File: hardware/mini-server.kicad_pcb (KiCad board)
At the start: 6 copper layers, 91 parts, among them J1 RJ45_Hanrun_HR911105A_Horizon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, J2 HDMI_A, J3 Micro_SD_Card, J5 AudioJack4, J6 USB_C_Receptacle, J7 USB_C_Receptacle, J8 USB_C_Receptacle, Q1 2N7002, U1 NT5CB256M16ER-FL, U2 RK3328, U3 TPD12S016PWR, U6 TPS563252DRLR, U7 TPS563252DRLR, U8 TPS563252DRLR, U9 TPS563252DRLR

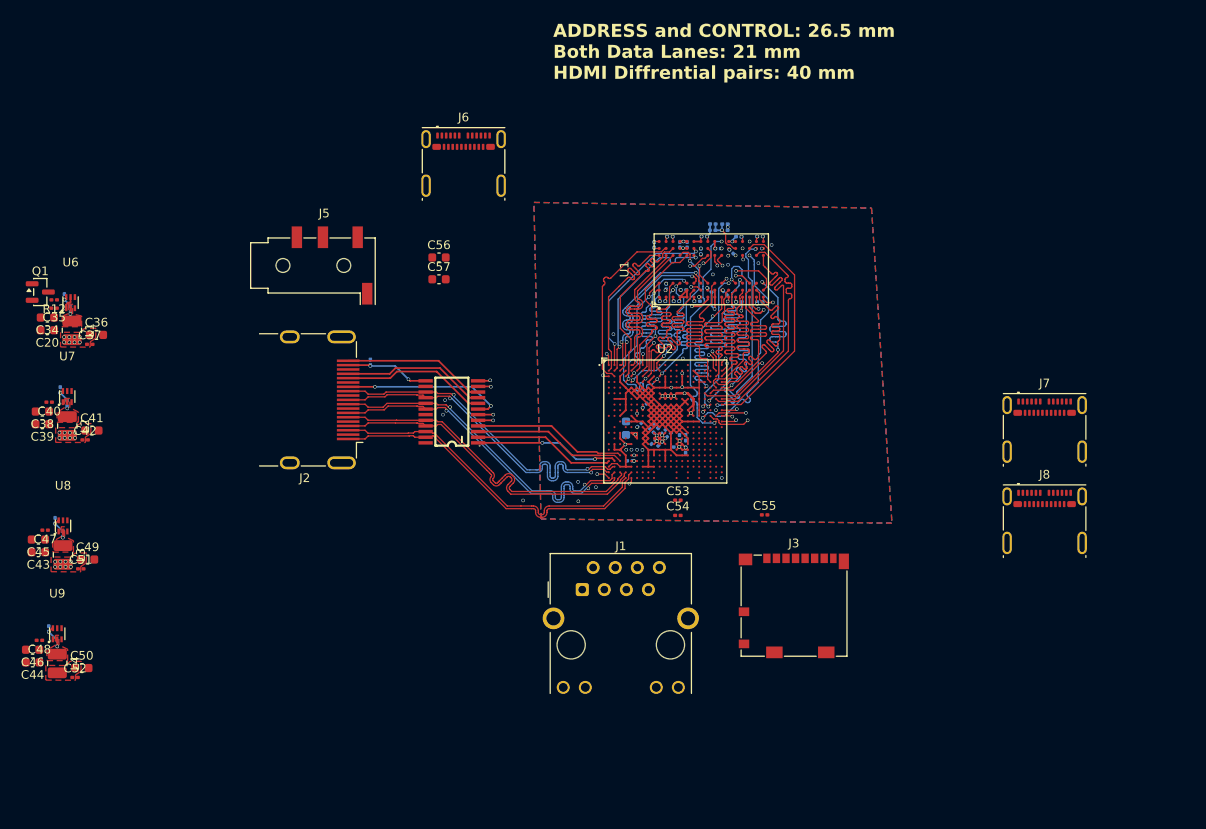
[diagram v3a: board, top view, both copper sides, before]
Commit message: component Placement
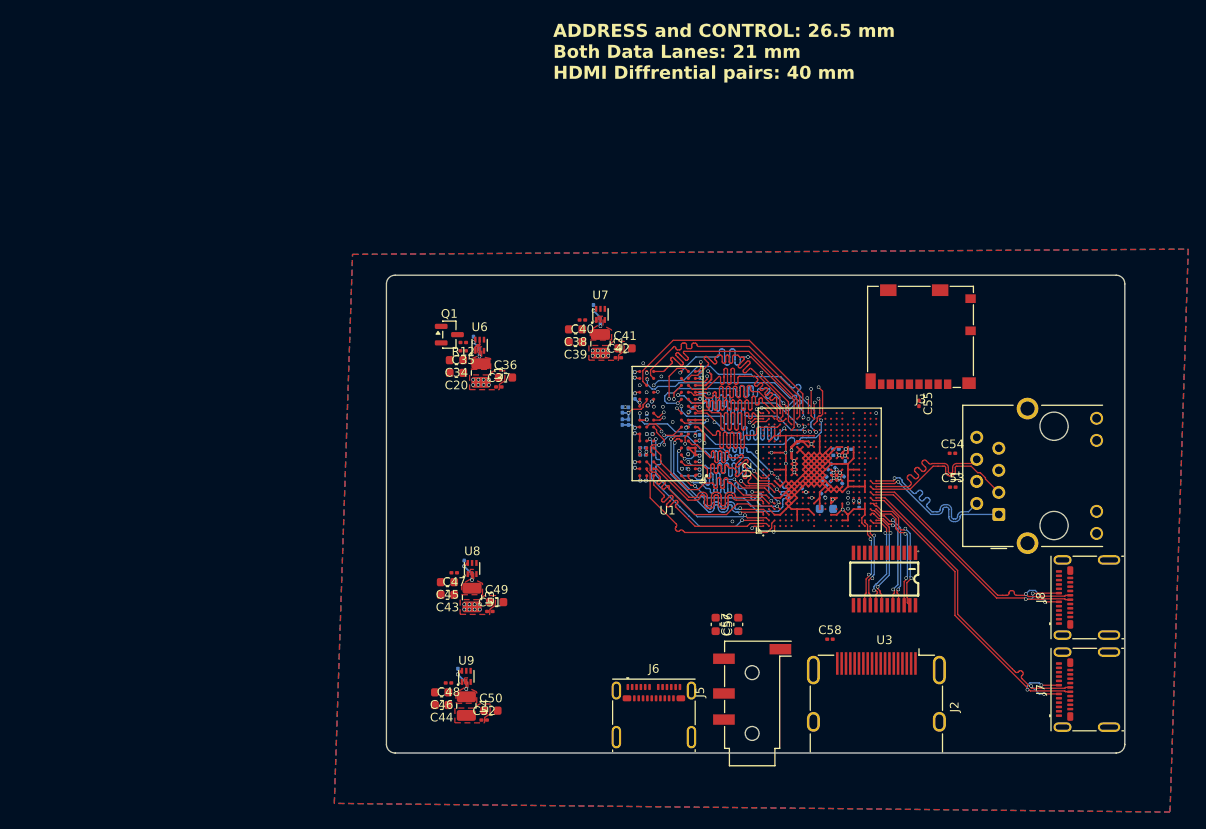
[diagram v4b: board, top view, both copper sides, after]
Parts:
- C58: moved to F.Cu
- moved J2 72.4 mm to (153.9, 122.4), turned to -90 degrees
- moved J5 69.6 mm to (139.6, 122.4), turned to 90 degrees
- moved J6 67.2 mm to (128.3, 125.0)
- moved C38 62.1 mm to (119.3, 80.6)
- moved C39 62.1 mm to (119.3, 82.1)
- moved C40 62.1 mm to (120.1, 79.6)
- moved U7 62.1 mm to (122.1, 78.9)
- moved C41 62.1 mm to (125.0, 82.8)
- moved C42 62.1 mm to (124.2, 83.9)
- moved L2 62.1 mm to (122.1, 82.3)
- moved R6 62.1 mm to (122.1, 79.7)
- moved R7 62.1 mm to (121.3, 78.2)
- moved C58 61.8 mm to (148.6, 116.3), turned to 0 degrees
- moved U3 53.4 mm to (154.8, 109.4), turned to 180 degrees
- moved C56 52.9 mm to (135.4, 114.6), turned to -90 degrees
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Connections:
- net /USB/USB2_0_DM renamed /USB/USB2_0_D-
- net /USB/USB2_0_DP renamed /USB/USB2_0_D+
- net /USB/USB2_1_DM renamed /USB/USB2_1_D-
- net /USB/USB2_1_DP renamed /USB/USB2_1_D+
- J7 pad A4: Net-(J7-VBUS-PadA4) -> VSYS
- J7 pad A9: Net-(J7-VBUS-PadA4) -> VSYS
- J7 pad B4: Net-(J7-VBUS-PadA4) -> VSYS
- J7 pad B9: Net-(J7-VBUS-PadA4) -> VSYS
- J8 pad A1: Net-(J8-GND-PadA1) -> GND
- J8 pad A12: Net-(J8-GND-PadA1) -> GND
- J8 pad B1: Net-(J8-GND-PadA1) -> GND
- J8 pad B12: Net-(J8-GND-PadA1) -> GND
- J8 pad SH: unconnected-(J8-SHIELD-PadSH) -> GND
- U1 pad J1: GND -> unconnected-(U1-NC-PadJ1)
- U2 pad AA15: unconnected-(U2E-GPIO1_B1/UART0_TX/GMAC_TXD0_M1-PadAA15) -> Net-(J4-Pin_2)
- U2 pad R1: unconnected-(U2H-XIN24M-PadR1) -> Net-(U2H-XIN24M)
- U2 pad T1: unconnected-(U2H-XOUT24M-PadT1) -> Net-(U2H-XOUT24M)
- U2 pad V13: unconnected-(U2E-GPIO1_B3/UART0_CTSN/GMAC_RXD0_M1-PadV13) -> Net-(U2E-GPIO1_B3/UART0_CTSN/GMAC_RXD0_M1)
- U2 pad W14: unconnected-(U2E-GPIO1_B2/UART0_RTSN/GMAC_RXD1_M1-PadW14) -> Net-(U2E-GPIO1_B2/UART0_RTSN/GMAC_RXD1_M1)
- U2 pad Y15: unconnected-(U2E-GPIO1_B0/UART0_RX/GMAC_TXD1_M1-PadY15) -> Net-(J4-Pin_3)
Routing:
- net /USB/USB2_0_D-: track 0.00 -> 39.7 mm, vias 0 -> 2
- net /USB/USB2_0_D+: track 0.00 -> 38.9 mm, vias 0 -> 2
- net /USB/USB2_1_D+: track 0.00 -> 32.8 mm, vias 0 -> 2
- net /USB/USB2_1_D-: track 0.00 -> 32.5 mm, vias 0 -> 2
- net /HDMI/HDMI_CLKP: track 39.0 -> 9.89 mm
- net /HDMI/HDMI_CLKN: track 39.5 -> 10.5 mm
- net /HDMI/HDMI_TX0P: track 39.4 -> 11.7 mm
- net /HDMI/HDMI_TX0N: track 39.5 -> 12.2 mm
- net /HDMI/HDMI_TX1P: track 39.9 -> 13.6 mm, vias 0 -> 2
- net /HDMI/HDMI_TX1N: track 39.2 -> 13.1 mm, vias 0 -> 2
- net /HDMI/HDMI_TX2N: track 38.7 -> 13.8 mm, vias 0 -> 2
- net /HDMI/HDMI_TX2P: track 40.0 -> 15.6 mm, vias 0 -> 2
- net Net-(J2-CEC): track 19.0 -> 0.00 mm, vias 2 -> 0
- net /Ethernet/PHY_RXP: track 0.00 -> 18.9 mm
- net /Ethernet/PHY_RXN: track 0.00 -> 18.9 mm
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- added copper zone on In3.Cu, net GND
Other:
- board outline added: 85 x 55 mm

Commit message: routing
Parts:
- added C60: C_Small, Capacitor_SMD:C_0201_0603Metric, F.Cu at (135.2, 106.9)
- added C61: C_Small, Capacitor_SMD:C_0201_0603Metric, F.Cu at (140.2, 105.9)
- added J4: Conn_01x04_Pin, Connector_PinHeader_2.54mm:PinHeader_1x04_P2.54mm_Vertical, F.Cu at (137.2, 77.4)
- added J9: USB_C_Receptacle, Connector_USB:USB_C_Receptacle_Molex_105450-0101, F.Cu at (107.9, 125.1)
- added R13: R, Resistor_SMD:R_0201_0603Metric, B.Cu at (140.7, 98.7)
- added R14: R, Resistor_SMD:R_0201_0603Metric, B.Cu at (132.9, 100.1)
- added R15: R, Resistor_SMD:R_0201_0603Metric, B.Cu at (141.1, 99.7)
- added TP1: ~{UART0_CTS}, TestPoint:TestPoint_Pad_D1.0mm, B.Cu at (138.9, 86.7)
- added TP2: ~{UART0_RST}, TestPoint:TestPoint_Pad_D1.0mm, B.Cu at (138.9, 84.2)
- added U4: BQ25887RGE, Package_DFN_QFN:Texas_RGE0024H_VQFN-24-1EP_4x4mm_P0.5mm_EP2.7x2.7mm, F.Cu at (102.5, 116.4)
- added Y1: Crystal_GND24, Crystal:Crystal_SMD_3225-4Pin_3.2x2.5mm, F.Cu at (137.7, 105.8)
- moved C50 58.3 mm to (167.8, 124.7)
- moved C52 58.3 mm to (167.1, 125.8)
- moved C44 58.3 mm to (162.2, 124.0)
- moved C46 58.3 mm to (162.2, 122.6)
- moved R10 58.3 mm to (165.0, 121.8)
- moved C48 58.3 mm to (163.0, 121.5)
- moved L4 58.3 mm to (165.0, 124.1)
- moved R11 58.3 mm to (164.0, 120.2)
- moved U9 58.3 mm to (165.0, 120.7)
- moved R12 23.7 mm to (110.5, 105.4)
- moved C20 23.7 mm to (109.8, 108.9)
- moved C34 23.7 mm to (109.8, 107.5)
- moved C35 23.7 mm to (110.5, 106.4)
- moved C36 23.7 mm to (115.4, 109.5)
- moved C37 23.7 mm to (114.6, 110.5)
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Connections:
- net /USB/USB3_DM renamed /USB/USB3_D-
- net /USB/USB3_DP renamed /USB/USB3_D+
- U2 pad H6: unconnected-(U2B-VCCIO6-PadH6) -> +3V3
- U2 pad R16: unconnected-(U2B-VCCIO5-PadR16) -> +3V3
- U2 pad T17: unconnected-(U2B-VCCIO2-PadT17) -> +3V3
- U2 pad U12: unconnected-(U2B-VCCIO4-PadU12) -> +3V3
- U2 pad U7: unconnected-(U2B-VCCIO3-PadU7) -> +3V3
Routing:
- net /Ethernet/PHY_LINK_LED: track 0.00 -> 46.1 mm, vias 0 -> 1
- net /Ethernet/PHY_DATA_LED: track 0.00 -> 43.0 mm, vias 0 -> 1
- net /Storage/SD_D2: track 0.00 -> 35.1 mm
- net /Storage/SD_D0: track 0.00 -> 35.0 mm
- net /Storage/SD_D1: track 0.00 -> 34.9 mm
- net /Storage/SD_CLK: track 0.00 -> 34.9 mm
- net /Storage/SD_CMD: track 0.00 -> 34.9 mm
- net /USB/USB3_RXN: track 0.00 -> 34.3 mm, vias 0 -> 2
- net /USB/USB3_RXP: track 0.00 -> 33.5 mm, vias 0 -> 2
- net /USB/USB3_D-: track 0.00 -> 30.9 mm, vias 0 -> 2
- net /USB/USB3_TXP: track 0.00 -> 30.6 mm
- net /USB/USB3_TXN: track 0.00 -> 30.4 mm
- net /USB/USB3_D+: track 0.00 -> 28.0 mm
- net /Storage/SD_D3: track 0.00 -> 27.2 mm, vias 0 -> 2
- net Net-(J4-Pin_2): track 0.00 -> 23.5 mm
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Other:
- board text added: "ADDRESS and CONTROL: 26.5 mm Both Data Lanes: 21 mm HDMI Diffrential pairs: 27.8 mm"
- board text removed: "ADDRESS and CONTROL: 26.5 mm Both Data Lanes: 21 mm HDMI Diffrential pairs: 40 mm"

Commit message: New battery charger IC
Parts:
- added C62: 100n, Capacitor_SMD:C_0201_0603Metric, F.Cu at (69.9, 107.3)
- added C63: 10u, Capacitor_SMD:C_0603_1608Metric, F.Cu at (79.5, 107.7)
- added C64: 100n, Capacitor_SMD:C_0201_0603Metric, F.Cu at (69.9, 109.1)
- added C65: 1u, Capacitor_SMD:C_0201_0603Metric, F.Cu at (69.9, 110.8)
- added C66: 10u, Capacitor_SMD:C_0603_1608Metric, F.Cu at (79.5, 110.2)
- added C67: 100n, Capacitor_SMD:C_0201_0603Metric, F.Cu at (69.9, 112.6)
- added C68: 1u, Capacitor_SMD:C_0201_0603Metric, F.Cu at (69.9, 114.3)
- added L5: 2.2u, Inductor_SMD:L_1008_2520Metric, F.Cu at (78.7, 114.3)
- added U5: BQ25690RBAR_C53283868, easyeda2kicad:WQFN-26_L4.0-W3.5_BQ25690RBAR, F.Cu at (74.5, 109.6)
- U4: value BQ25887RGE -> TPS565201; footprint Package_DFN_QFN:Texas_RGE0024H_VQFN-24-1EP_4x4mm_P0.5mm_EP2.7x2.7mm -> Package_TO_SOT_SMD:SOT-23-6
- moved U4 28.9 mm to (73.7, 114.8), turned to 0 degrees
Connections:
- J9 pad A4: Net-(U4-VBUS) -> VBUS
- J9 pad A9: Net-(U4-VBUS) -> VBUS
- J9 pad B4: Net-(U4-VBUS) -> VBUS
- J9 pad B9: Net-(U4-VBUS) -> VBUS
- U4 pad 1: unconnected-(U4-~{PG}-Pad1) -> GND
- U4 pad 2: unconnected-(U4-STAT-Pad2) -> Net-(U4-SW)
- U4 pad 3: unconnected-(U4-CD-Pad3) -> Net-(U4-EN)
- U4 pad 4: unconnected-(U4-SDA-Pad4) -> Net-(U4-FB)
- U4 pad 5: unconnected-(U4-SCL-Pad5) -> Net-(U4-EN)
- U4 pad 6: unconnected-(U4-~{INT}-Pad6) -> Net-(U4-VBST)
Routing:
- net VBUS: track 0.00 -> 6.53 mm
- net Net-(U4-VBUS): track 6.53 -> 0.00 mm
